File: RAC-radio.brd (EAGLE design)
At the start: 25.4 x 50.8 mm, 24 parts, among them J2 CORTEX_DEBUG_MINIMUM_SMD, J3 U.FL, U1 MAX32660GTP+, U2 RN4871-I_RM130, U3 RFM95W-868S2, Y1 32.768kHz

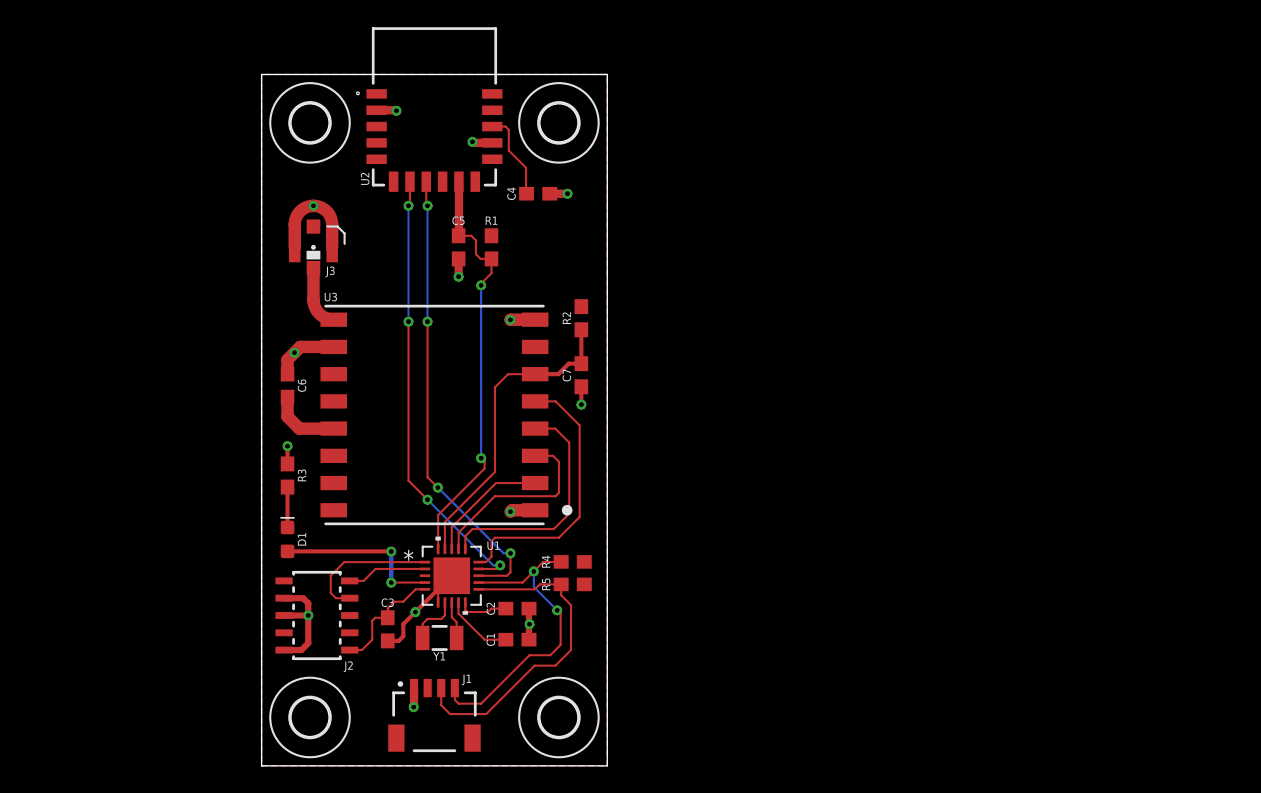
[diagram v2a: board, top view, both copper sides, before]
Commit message: Started anew with the SIM7000 LTE-M/GPS module
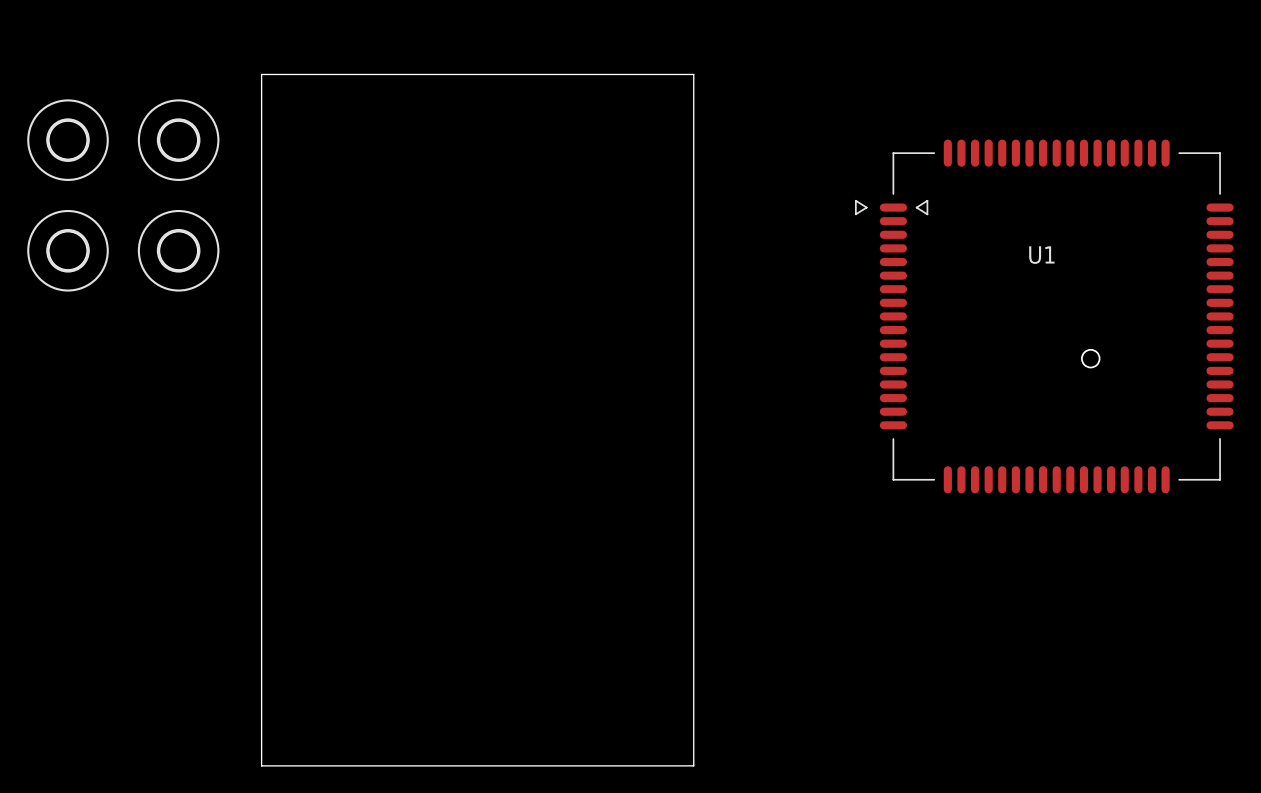
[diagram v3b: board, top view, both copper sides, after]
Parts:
- removed C1, C2: 1.0uF, SparkFun-Capacitors:0603
- removed C3, C5, C7: 0.1uF, SparkFun-Capacitors:0603
- removed C4, C6: 10uF, SparkFun-Capacitors:0603
- removed D1: (no value), SparkFun-LED:LED-0603
- removed J1: (no value), SparkFun-Connectors:JST04_1MM_RA
- removed J2: CORTEX_DEBUG_MINIMUM_SMD, SparkFun-Connectors:SAMTECH_FTSH-105-01
- removed J3: U.FL, SparkFun-Connectors:U.FL
- removed R1, R2: 10k, SparkFun-Resistors:0603
- removed R3: 470, SparkFun-Resistors:0603
- removed R4, R5: 4.7k, SparkFun-Resistors:0603
- removed U2: RN4871-I_RM130, RAC-Altimeter:RN4871
- removed U3: RFM95W-868S2, RAC-Altimeter:XCVR_RFM95W-868S2
- removed Y1: 32.768kHz, SparkFun-Clocks:CRYSTAL-SMD-3.2X1.5MM
- U1: value MAX32660GTP+ -> (none); device RAC-Altimeter:21-0139V_T2044+5 -> rocket-components:SIM7000
- moved U1 48.4 mm to (58.4, 33.0)
- moved H4 44.2 mm to (-6.10, 37.8)
- moved H3 38.6 mm to (-14.2, 37.8)
- moved H2 28.0 mm to (-6.10, 46.0)
- moved H1 17.8 mm to (-14.2, 46.0)
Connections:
- removed net !BT_RST: C5.1, R1.1, U1.20, U2.10
- removed net !LORA_RST: C7.1, R2.1, U1.19, U3.6
- removed net !MCU_RST: C3.1, J2.10, U1.5
- removed net !SPI0_CS: U1.15, U3.5
- removed net 32KIN: U1.8, Y1.P$1
- removed net 32KOUT: U1.7, Y1.P$2
- removed net GND: C1.2, C2.2, C3.2, C4.2, C5.2, C6.2, C7.2, J1.1, J2.3, J2.5, J2.9, J3.1, J3.2, R3.2, U1.21, U1.6, U2.13, U2.2, U3.1, U3.10, U3.8
- removed net I2C0_SCL: J1.4, R4.1, U1.12
- removed net I2C0_SDA: J1.3, R5.1, U1.11
- removed net IO_LED: D1.A, U1.4
- removed net LED_CATH: D1.C, R3.1
- removed net LORA_ANT: J3.FEED, U3.9
- removed net SPI0_MISO: U1.18, U3.2
- removed net SPI0_MOSI: U1.17, U3.3
- removed net SPI0_SCK: U1.16, U3.4
- removed net SWDCLK: J2.4, U1.1
- removed net SWDIO: J2.2, U1.2
- removed net UART1_RX: U1.13, U2.8
- removed net UART1_TX: U1.14, U2.7
- removed net VCC: C1.1, C4.1, C6.1, J1.2, J2.1, R1.2, R2.2, R4.2, R5.2, U1.9, U2.14, U3.13
- removed net VCORE: C2.1, U1.10
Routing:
- net GND: track 45.9 -> 0.00 mm, vias 14 -> 0
- net UART1_RX: track 34.0 -> 0.00 mm, vias 4 -> 0
- net UART1_TX: track 33.0 -> 0.00 mm, vias 4 -> 0
- net !BT_RST: track 30.8 -> 0.00 mm, vias 2 -> 0
- net I2C0_SDA: track 24.4 -> 0.00 mm
- net I2C0_SCL: track 23.5 -> 0.00 mm, vias 2 -> 0
- net !LORA_RST: track 23.0 -> 0.00 mm
- net !SPI0_CS: track 20.2 -> 0.00 mm
- net SPI0_SCK: track 17.4 -> 0.00 mm
- net VCC: track 16.8 -> 0.00 mm
- net SPI0_MOSI: track 14.0 -> 0.00 mm
- net IO_LED: track 12.4 -> 0.00 mm, vias 2 -> 0
- net SWDCLK: track 10.2 -> 0.00 mm
- net SPI0_MISO: track 9.07 -> 0.00 mm
- net !MCU_RST: track 8.59 -> 0.00 mm
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- removed copper zone on layer 16, net GND
- removed copper zone on layer 1, net VCC
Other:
- board size 25.4 x 50.8 mm -> 31.8 x 50.8 mm
